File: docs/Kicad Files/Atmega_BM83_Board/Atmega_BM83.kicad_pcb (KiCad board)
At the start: 2 copper layers, 114.3 x 88.9 mm, 35 parts, among them J1 18V, J10 ICE Header, J2 Out to Amp, J3 PWR SW, J4 Volume POT, J5 Pairing BTN, J6 PWR LED, J7 Pair LED, J8 Conn_01x12, J9 Conn_01x12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

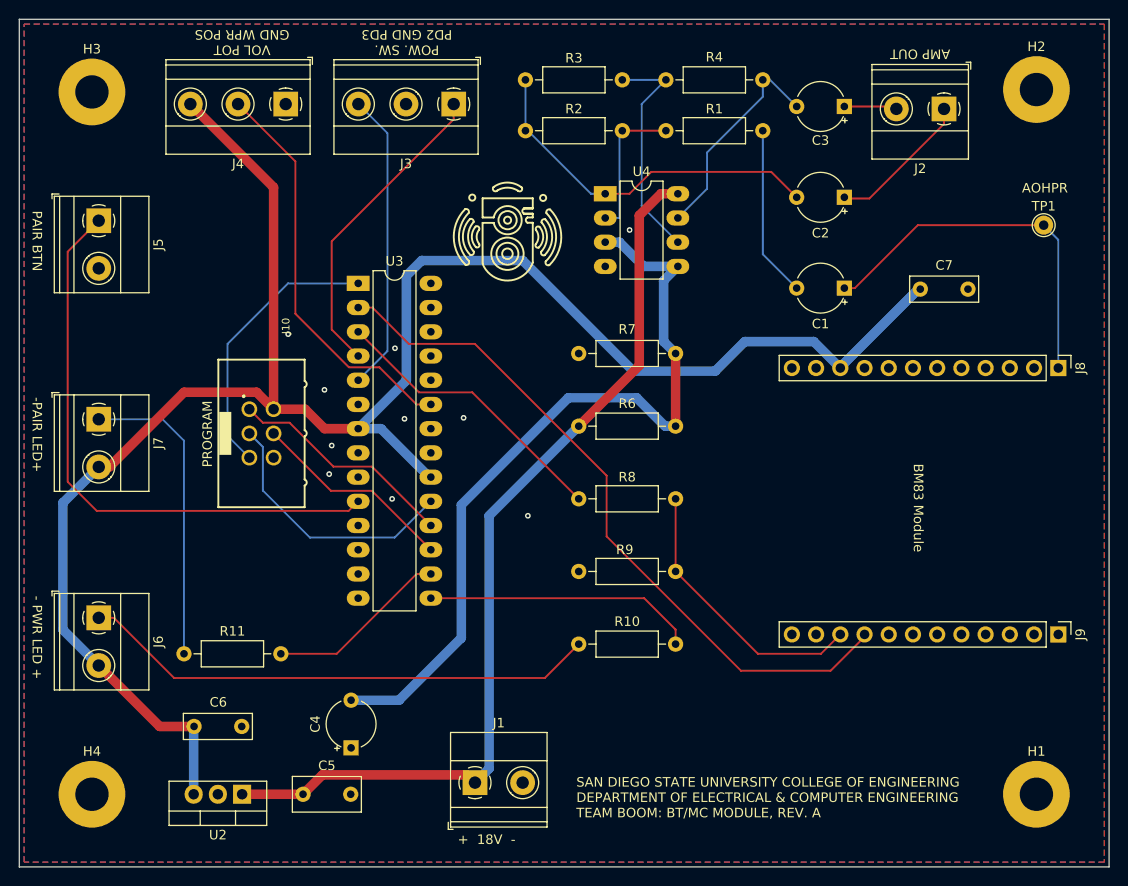
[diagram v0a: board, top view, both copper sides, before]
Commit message: updated BT/MC board to reflect changes: removed C2 and C3, changed some cap locations
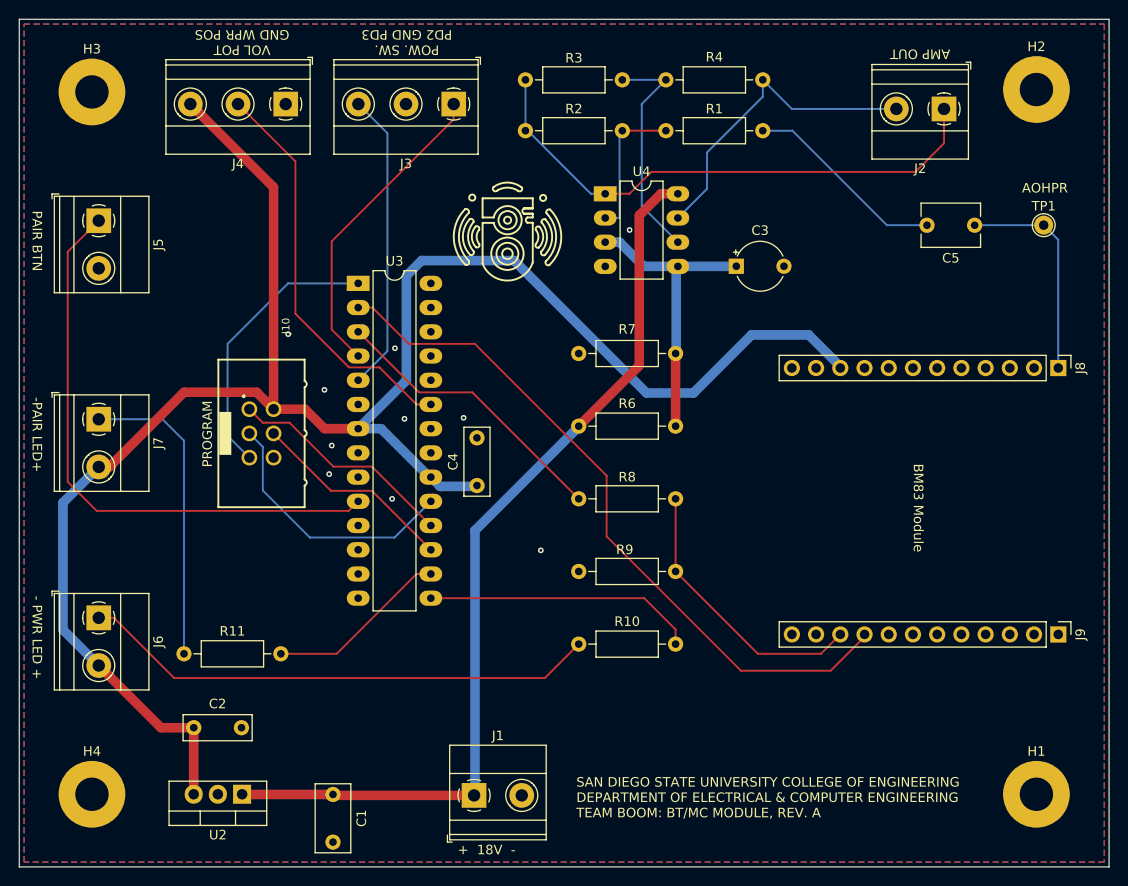
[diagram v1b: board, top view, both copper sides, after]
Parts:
- removed C6, C7: 0.1uF, Capacitor_THT:C_Rect_L7.0mm_W2.5mm_P5.00mm
- C2, C4: value 10uF -> 0.1uF; footprint Capacitor_THT:CP_Radial_Tantal_D5.0mm_P5.00mm -> Capacitor_THT:C_Rect_L7.0mm_W2.5mm_P5.00mm
- C5: renamed from C1; footprint Capacitor_THT:CP_Radial_Tantal_D5.0mm_P5.00mm -> Capacitor_THT:C_Disc_D6.0mm_W4.4mm_P5.00mm
- moved C2 88.0 mm to (69.1, 137.8), turned to 0 degrees
- moved C4 30.5 mm to (98.8, 112.4)
- moved C3 20.2 mm to (126.0, 89.4), turned to 0 degrees
- moved C5 15.2 mm to (151.0, 85.1)
- moved C1 3.14 mm to (83.7, 144.8), turned to -90 degrees
- moved J1 1.34 mm to (98.5, 144.9)
- renumbered C5 to C1
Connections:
- C2 pad 1: Net-(J2-Pin_1) -> 5V
- C2 pad 2: Net-(C2-Pad2) -> GND
- C3 pad 1: Net-(J2-Pin_2) -> 8V
- C3 pad 2: Net-(C3-Pad2) -> GND
- C4 pad 1: GND -> 5V
- C4 pad 2: 8V -> GND
- R2 pad 2: Net-(C2-Pad2) -> Net-(J2-Pin_1)
- R3 pad 2: Net-(C2-Pad2) -> Net-(J2-Pin_1)
- R4 pad 2: Net-(C3-Pad2) -> Net-(J2-Pin_2)
- U4 pad 1: Net-(C2-Pad2) -> Net-(J2-Pin_1)
- U4 pad 7: Net-(C3-Pad2) -> Net-(J2-Pin_2)
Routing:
- net 8V: track 83.2 -> 31.8 mm
- net Net-(J2-Pin_1): track 15.3 -> 57.8 mm
- net Net-(C2-Pad2): track 38.6 -> 0.00 mm
- net Net-(J2-Pin_2): track 5.56 -> 33.4 mm
- net Net-(C3-Pad2): track 22.9 -> 0.00 mm
- net AOHPR: track 39.3 -> 22.9 mm
- net 5V: track 205.2 -> 200.7 mm
- net Net-(C5-Pad2): track 18.0 -> 21.3 mm
- net 18V: track 97.2 -> 96.0 mm
